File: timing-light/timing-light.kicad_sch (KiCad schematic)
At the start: 35 parts

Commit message: [timing-light] update
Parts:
- removed R8: (no value), symbol Device:R
- added Cpwr1: 0.33u, symbol Device:C
- added Cpwr2: 0.1u, symbol Device:C
- added D5: BAT42, Diode_THT:D_DO-35_SOD27_P7.62mm_Horizontal, symbol Diode:BAT42
- added RV1: 470k, Connector_Wire:SolderWire-0.15sqmm_1x03_P4mm_D0.5mm_OD1.5mm, symbol Device:R_Potentiometer
- added SWfreq1: SW_SPDT, Connector_Wire:SolderWire-0.15sqmm_1x03_P4mm_D0.5mm_OD1.5mm, symbol Switch:SW_SPDT
- added U_pwr1: L7805, symbol Regulator_Linear:L7805
- C1: value (none) -> 68pF; footprint (none) -> Capacitor_THT:C_Disc_D3.8mm_W2.6mm_P2.50mm
- C2, C_ign1, C_u1, C_u_dr1: value (none) -> 0.1uF; footprint (none) -> Capacitor_THT:C_Disc_D3.8mm_W2.6mm_P2.50mm
- C3: value (none) -> C
- D1, D2, D3, D4: value (none) -> 1.5KExxA; footprint (none) -> Diode_THT:D_DO-201AE_P15.24mm_Horizontal
- J1, J_coil1, J_light1, J_light2, J_sens_out1: value (none) -> Conn_01x02_Male; footprint (none) -> Connector_Wire:SolderWire-0.75sqmm_1x02_P7mm_D1.25mm_OD3.5mm
- J2, J_pwr1, J_sens_in1: value (none) -> Conn_01x02_Female; footprint (none) -> Connector_Wire:SolderWire-0.75sqmm_1x02_P7mm_D1.25mm_OD3.5mm
- J_input_clamp1: value (none) -> Conn_01x01_Female; footprint (none) -> Connector_Wire:SolderWire-0.75sqmm_1x01_D1.25mm_OD3.5mm
- Q1, Q2: value (none) -> IRFB3004PbF; footprint (none) -> MY_LIB:TO-220-3-4_Horizontal_TabDown
- R1: value (none) -> 15k; footprint (none) -> Resistor_THT:R_Axial_DIN0204_L3.6mm_D1.6mm_P5.08mm_Horizontal
- R2: value (none) -> 3k; footprint (none) -> Resistor_THT:R_Axial_DIN0204_L3.6mm_D1.6mm_P5.08mm_Horizontal
- R3: value (none) -> 1k/4.7k; footprint (none) -> Resistor_THT:R_Axial_DIN0204_L3.6mm_D1.6mm_P5.08mm_Horizontal
- R4: value (none) -> 100k; footprint (none) -> Resistor_THT:R_Axial_DIN0204_L3.6mm_D1.6mm_P5.08mm_Horizontal
- R5, R_light1: value (none) -> R; footprint (none) -> Resistor_THT:R_Axial_DIN0204_L3.6mm_D1.6mm_P5.08mm_Horizontal
- R6, R7: value (none) -> 1k; footprint (none) -> Resistor_THT:R_Axial_DIN0204_L3.6mm_D1.6mm_P5.08mm_Horizontal
- SW_ign1: value (none) -> SW_SPST; footprint (none) -> Connector_Wire:SolderWire-0.75sqmm_1x02_P7mm_D1.25mm_OD3.5mm
- TP1: value (none) -> TestPoint; footprint (none) -> Connector_Wire:SolderWire-0.75sqmm_1x01_D1.25mm_OD2.3mm
- U1: value (none) -> 4001; footprint (none) -> Package_DIP:DIP-14_W7.62mm_Socket
- U_dr1: value (none) -> LDB600; footprint (none) -> MY_LIB:MEANWELL_LDB-350L
- U_ign1: value (none) -> TLC555xP; footprint (none) -> Package_DIP:DIP-8_W7.62mm
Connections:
- net +12V: now also Cpwr1.1, Cpwr2.1, U_pwr1.1 (IN), U_pwr1.3 (OUT)
- net GND: now also Cpwr1.2, Cpwr2.2, U_pwr1.2 (GND)
- net at R5.2, TP1.1, U_ign1.3 (Q): now also D5.2 (A); no longer R6.1, R7.1
- net Uign_dis: now reaches U_ign1.7 (DIS)
- net Uign_dis: now also R7.2
- net at R6.2: now also RV1.3
- net U_ign_tr renamed Uign_trig
- net Uign_trig: now also RV1.2, SWfreq1.2 (B); no longer C3.1, R7.2
- new net: R7.1, RV1.1
- new net: D5.1 (K), R6.1
- new net: C3.1, SWfreq1.3 (C)
- no-connect marks 2 -> 1
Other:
- note added: "C3 = 680n + 100n => 3.93 Hz ~ 471.36 RPM 330n + 33n => 8.44 Hz ~ 1012.84 RPM 150n + 33n => 16.74 Hz ~ 2009.07 RPM"
- note added: "INPUT CLAMP"
- note added: "Not really LDB600 but any suitable LED driver"
- note added: "TESTER"
- note added: "f = 1.44 / (RV1 * C) Q = var"
- note removed: "(15k || (68k + 15k) = 12.70k) => f = 8.337Hz = 1000.46 об/мин"
- note removed: "f = 0.72 / (R_var*C) Q = 0.5"
- moved on the sheet: J1, R5, SW_ign1, TP1, U_ign1

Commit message: [timing-light] Use BU941ZP as ignition coil driver
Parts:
- removed Q1: IRFB3004PbF, MY_LIB:TO-220-3-4_Horizontal_TabDown, symbol timing-light-rescue:IRFB3004PbF-IRFB3004PbF
- added CR1: BU941ZPFI, LIB:BU941ZPFI, symbol 2022-09-04_19-09-05:BU941ZPFI
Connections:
- net GND: now also CR1.3 (E)
- net at J2.2 (Pin_2): now also CR1.1 (B)
- net at D1.2 (A2), D2.1 (A1), J_coil1.2 (Pin_2): now also CR1.2 (C)
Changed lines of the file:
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@@
   (junction (at 165.1 38.1) (diameter 0) (color 0 0 0 0)
   )
+  (junction (at 157.48 72.39) (diameter 0) (color 0 0 0 0)
+  )
+  (junction (at 255.27 93.98) (diameter 0) (color 0 0 0 0)
+  )
+  (junction (at 237.49 86.36) (diameter 0) (color 0 0 0 0)
+  )
+  (junction (at 193.04 35.56) (diameter 0) (color 0 0 0 0)
+  )
+  (junction (at 269.24 86.36) (diameter 0) (color 0 0 0 0)
+  )
+  (junction (at 74.93 168.91) (diameter 0) (color 0 0 0 0)
+  )
+  (junction (at 109.22 111.76) (diameter 0) (color 0 0 0 0)
+  )
+  (junction (at 86.36 158.75) (diameter 0) (color 0 0 0 0)
+  )
+  (junction (at 146.05 72.39) (diameter 0) (color 0 0 0 0)
+  )
+  (junction (at 68.58 30.48) (diameter 0) (color 0 0 0 0)
+  )
+  (junction (at 193.04 31.75) (diameter 0) (color 0 0 0 0)
+  )
   (junction (at 62.23 158.75) (diameter 0) (color 0 0 0 0)
-  )
-  (junction (at 157.48 72.39) (diameter 0) (color 0 0 0 0)
-  )
-  (junction (at 255.27 93.98) (diameter 0) (color 0 0 0 0)
-  )
-  (junction (at 237.49 86.36) (diameter 0) (color 0 0 0 0)
-  )
-  (junction (at 193.04 35.56) (diameter 0) (color 0 0 0 0)
-  )
-  (junction (at 269.24 86.36) (diameter 0) (color 0 0 0 0)
-  )
-  (junction (at 74.93 168.91) (diameter 0) (color 0 0 0 0)
-  )
-  (junction (at 109.22 111.76) (diameter 0) (color 0 0 0 0)
-  )
-  (junction (at 64.77 158.75) (diameter 0) (color 0 0 0 0)
-  )
-  (junction (at 86.36 158.75) (diameter 0) (color 0 0 0 0)
-  )
-  (junction (at 146.05 72.39) (diameter 0) (color 0 0 0 0)
-  )
-  (junction (at 68.58 30.48) (diameter 0) (color 0 0 0 0)
-  )
-  (junction (at 193.04 31.75) (diameter 0) (color 0 0 0 0)
   )
   (junction (at 170.18 58.42) (diameter 0) (color 0 0 0 0)
@@
     (stroke (width 0) (type default) (color 0 0 0 0))
   )
-  (wire (pts (xy 64.77 158.75) (xy 86.36 158.75))
-    (stroke (width 0) (type default) (color 0 0 0 0))
-  )
   (wire (pts (xy 62.23 100.33) (xy 62.23 106.68))
     (stroke (width 0) (type default) (color 0 0 0 0))
@@
     (stroke (width 0) (type default) (color 0 0 0 0))
   )
-  (wire (pts (xy 62.23 158.75) (xy 64.77 158.75))
+  (wire (pts (xy 62.23 158.75) (xy 86.36 158.75))
     (stroke (width 0) (type default) (color 0 0 0 0))
   )
@@
     (pin "1")
   )
-  (symbol (lib_id "timing-light-rescue:IRFB3004PbF-IRFB3004PbF") (at 62.23 163.83 0) (unit 1)
-    (in_bom yes) (on_board yes)
-    (property "Reference" "Q1" (id 0) (at 66.2432 162.6616 0)
-      (effects (font (size 1.27 1.27)) (justify left))
-    )
-    (property "Value" "IRFB3004PbF" (id 1) (at 66.2432 164.973 0)
-      (effects (font (size 1.27 1.27)) (justify left))
-    )
-    (property "Footprint" "MY_LIB:TO-220-3-4_Horizontal_TabDown" (id 2) (at 66.04 167.64 0)
-      (effects (font (size 1.27 1.27)) hide)
-    )
-    (property "Datasheet" "" (id 3) (at 66.04 167.64 0)
-      (effects (font (size 1.27 1.27)) hide)
-    )
-    (pin "1")
-    (pin "2")
-    (pin "3")
-    (pin "4")
-  )
   (symbol (lib_id "power:VCC") (at 36.83 99.06 0) (unit 1)
     (in_bom yes) (on_board yes)
@@
     (property "Datasheet" "~" (id 3) (at 109.22 133.35 0)
       (effects (font (size 1.27 1.27)) hide)
+    )
+    (pin "1")
+    (pin "2")
+    (pin "3")
+  )
+  (symbol (lib_id "2022-09-04_19-09-05:BU941ZPFI") (at 54.61 163.83 0) (unit 1)
+    (in_bom yes) (on_board yes) (fields_autoplaced)
+    (property "Reference" "CR1" (id 0) (at 64.77 162.56 0)
+      (effects (font (size 1.524 1.524)) (justify left))
+    )
+    (property "Value" "BU941ZPFI" (id 1) (at 64.77 166.37 0)
+      (effects (font (size 1.524 1.524)) (justify left))
+    )
+    (property "Footprint" "LIB:BU941ZPFI" (id 2) (at 64.77 170.434 0)
+      (effects (font (size 1.524 1.524)) hide)
+    )
+    (property "Datasheet" "" (id 3) (at 54.61 163.83 0)
+      (effects (font (size 1.524 1.524)))
     )
     (pin "1")
@@
       (reference "C3") (unit 1) (value "C") (footprint "")
     )
+    (path "/a0c19b29-cc59-4b8d-b62d-b3bc4fc304b4"
+      (reference "CR1") (unit 1) (value "BU941ZPFI") (footprint "LIB:BU941ZPFI")
+    )
     (path "/00000000-0000-0000-0000-000062127850"
       (reference "C_ign1") (unit 1) (value "0.1uF") (footprint "Capacitor_THT:C_Disc_D3.8mm_W2.6mm_P2.50mm")
@@
       (reference "J_sens_out1") (unit 1) (value "Conn_01x02_Male") (footprint "Connector_Wire:SolderWire-0.75sqmm_1x02_P7mm_D1.25mm_OD3.5mm")
     )
-    (path "/00000000-0000-0000-0000-000062067b10"
-      (reference "Q1") (unit 1) (value "IRFB3004PbF") (footprint "MY_LIB:TO-220-3-4_Horizontal_TabDown")
-    )
     (path "/00000000-0000-0000-0000-00006210cd5e"

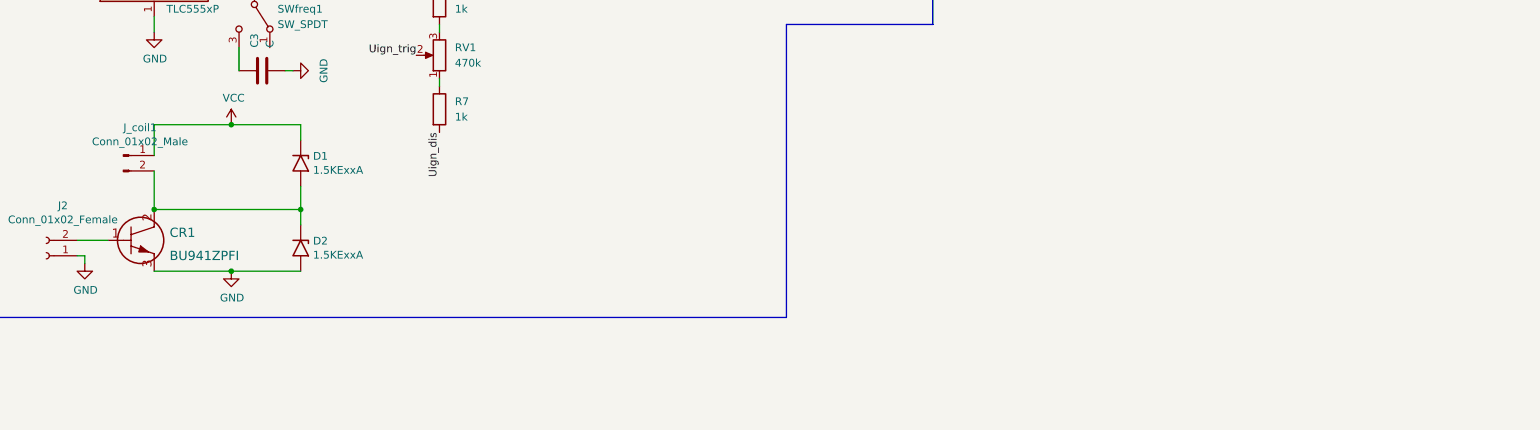
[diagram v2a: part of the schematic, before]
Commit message: [timing-light] Use add BU941ZP for update later
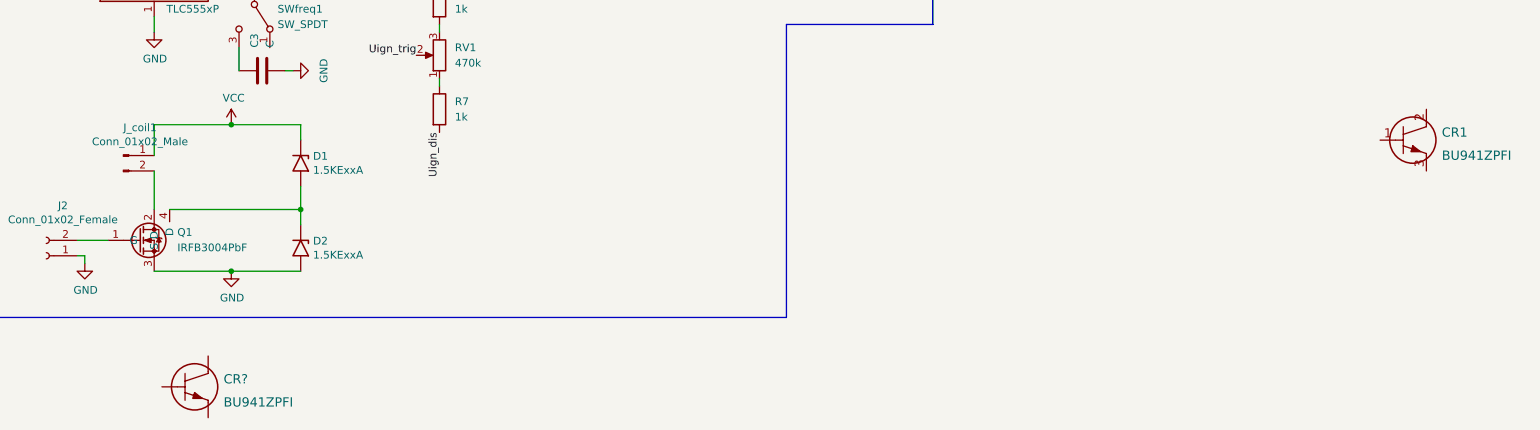
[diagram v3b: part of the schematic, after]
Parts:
- added CR?: BU941ZPFI, TO-3PF_STM, symbol 2022-09-04_19-09-05:BU941ZPFI
- added Q1: IRFB3004PbF, symbol IRFB3004PbF:IRFB3004PbF
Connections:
- net GND: now also Q1.3 (S); no longer CR1.3 (E)
- net at D1.2 (A2), D2.1 (A1): now also Q1.4 (D); no longer CR1.2 (C), J_coil1.2 (Pin_2)
- net at J2.2 (Pin_2): now also Q1.1 (G); no longer CR1.1 (B)
- new net: J_coil1.2 (Pin_2), Q1.2 (D)
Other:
- moved on the sheet: CR1
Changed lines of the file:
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@@
   (junction (at 193.04 31.75) (diameter 0) (color 0 0 0 0)
-  )
-  (junction (at 62.23 158.75) (diameter 0) (color 0 0 0 0)
   )
   (junction (at 170.18 58.42) (diameter 0) (color 0 0 0 0)
@@
     (stroke (width 0) (type default) (color 0 0 0 0))
   )
+  (wire (pts (xy 64.77 158.75) (xy 86.36 158.75))
+    (stroke (width 0) (type default) (color 0 0 0 0))
+  )
   (wire (pts (xy 269.24 21.59) (xy 269.24 24.13))
     (stroke (width 0) (type default) (color 0 0 0 0))
@@
   )
   (wire (pts (xy 74.93 144.78) (xy 86.36 144.78))
-    (stroke (width 0) (type default) (color 0 0 0 0))
-  )
-  (wire (pts (xy 62.23 158.75) (xy 86.36 158.75))
     (stroke (width 0) (type default) (color 0 0 0 0))
   )
@@
     (pin "1")
   )
+  (symbol (lib_name "BU941ZPFI_1") (lib_id "2022-09-04_19-09-05:BU941ZPFI") (at 63.5 187.96 0) (unit 1)
+    (in_bom yes) (on_board yes) (fields_autoplaced)
+    (property "Reference" "CR?" (id 0) (at 73.66 186.69 0)
+      (effects (font (size 1.524 1.524)) (justify left))
+    )
+    (property "Value" "BU941ZPFI" (id 1) (at 73.66 190.5 0)
+      (effects (font (size 1.524 1.524)) (justify left))
+    )
+    (property "Footprint" "TO-3PF_STM" (id 2) (at 73.66 194.564 0)
+      (effects (font (size 1.524 1.524)) hide)
+    )
+    (property "Datasheet" "" (id 3) (at 63.5 187.96 0)
+      (effects (font (size 1.524 1.524)))
+    )
+    (pin "1")
+    (pin "2")
+    (pin "3")
+  )
   (symbol (lib_id "Device:R") (at 109.22 142.24 0) (unit 1)
     (in_bom yes) (on_board yes) (fields_autoplaced)
@@
     (pin "3")
   )
-  (symbol (lib_id "2022-09-04_19-09-05:BU941ZPFI") (at 54.61 163.83 0) (unit 1)
+  (symbol (lib_id "2022-09-04_19-09-05:BU941ZPFI") (at 264.16 147.32 0) (unit 1)
     (in_bom yes) (on_board yes) (fields_autoplaced)
-    (property "Reference" "CR1" (id 0) (at 64.77 162.56 0)
+    (property "Reference" "CR1" (id 0) (at 274.32 146.05 0)
       (effects (font (size 1.524 1.524)) (justify left))
     )
-    (property "Value" "BU941ZPFI" (id 1) (at 64.77 166.37 0)
+    (property "Value" "BU941ZPFI" (id 1) (at 274.32 149.86 0)
       (effects (font (size 1.524 1.524)) (justify left))
     )
-    (property "Footprint" "LIB:BU941ZPFI" (id 2) (at 64.77 170.434 0)
+    (property "Footprint" "LIB:BU941ZPFI" (id 2) (at 274.32 153.924 0)
       (effects (font (size 1.524 1.524)) hide)
     )
-    (property "Datasheet" "" (id 3) (at 54.61 163.83 0)
+    (property "Datasheet" "" (id 3) (at 264.16 147.32 0)
       (effects (font (size 1.524 1.524)))
     )
@@
     (pin "1")
     (pin "2")
+  )
+  (symbol (lib_id "IRFB3004PbF:IRFB3004PbF") (at 62.23 163.83 0) (unit 1)
+    (in_bom yes) (on_board yes) (fields_autoplaced)
+    (property "Reference" "Q1" (id 0) (at 66.04 162.4964 0)
+      (effects (font (size 1.27 1.27)) (justify left))
+    )
+    (property "Value" "IRFB3004PbF" (id 1) (at 66.04 165.0364 0)
+      (effects (font (size 1.27 1.27)) (justify left))
+    )
+    (property "Footprint" "" (id 2) (at 66.04 167.64 0)
+      (effects (font (size 1.27 1.27)) hide)
+    )
+    (property "Datasheet" "" (id 3) (at 66.04 167.64 0)
+      (effects (font (size 1.27 1.27)) hide)
+    )
+    (pin "1")
+    (pin "2")
+    (pin "3")
+    (pin "4")
   )
   (symbol (lib_id "Device:R") (at 109.22 124.46 0) (unit 1)
@@
       (reference "CR1") (unit 1) (value "BU941ZPFI") (footprint "LIB:BU941ZPFI")
     )
+    (path "/07c9a077-4bb3-44c3-8d2c-d57c64b0e04b"
+      (reference "CR?") (unit 1) (value "BU941ZPFI") (footprint "TO-3PF_STM")
+    )
     (path "/00000000-0000-0000-0000-000062127850"
       (reference "C_ign1") (unit 1) (value "0.1uF") (footprint "Capacitor_THT:C_Disc_D3.8mm_W2.6mm_P2.50mm")
@@
       (reference "J_sens_out1") (unit 1) (value "Conn_01x02_Male") (footprint "Connector_Wire:SolderWire-0.75sqmm_1x02_P7mm_D1.25mm_OD3.5mm")
     )
+    (path "/ce21fc61-516f-4c07-8327-8dc880b2e513"
+      (reference "Q1") (unit 1) (value "IRFB3004PbF") (footprint "")
+    )
     (path "/00000000-0000-0000-0000-00006210cd5e"
